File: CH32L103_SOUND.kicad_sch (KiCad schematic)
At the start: 44 parts, among them J1 USB_C_Receptacle_PowerOnly_6P, J2 Conn_01x04, J3 Conn_01x05, J4 Conn_01x02, Q1 AO3400A, U1 USBLC6-2SC6, U2 TP4057, U3 HT7533-1, U4 CS588, U5 CH32L103F8U6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

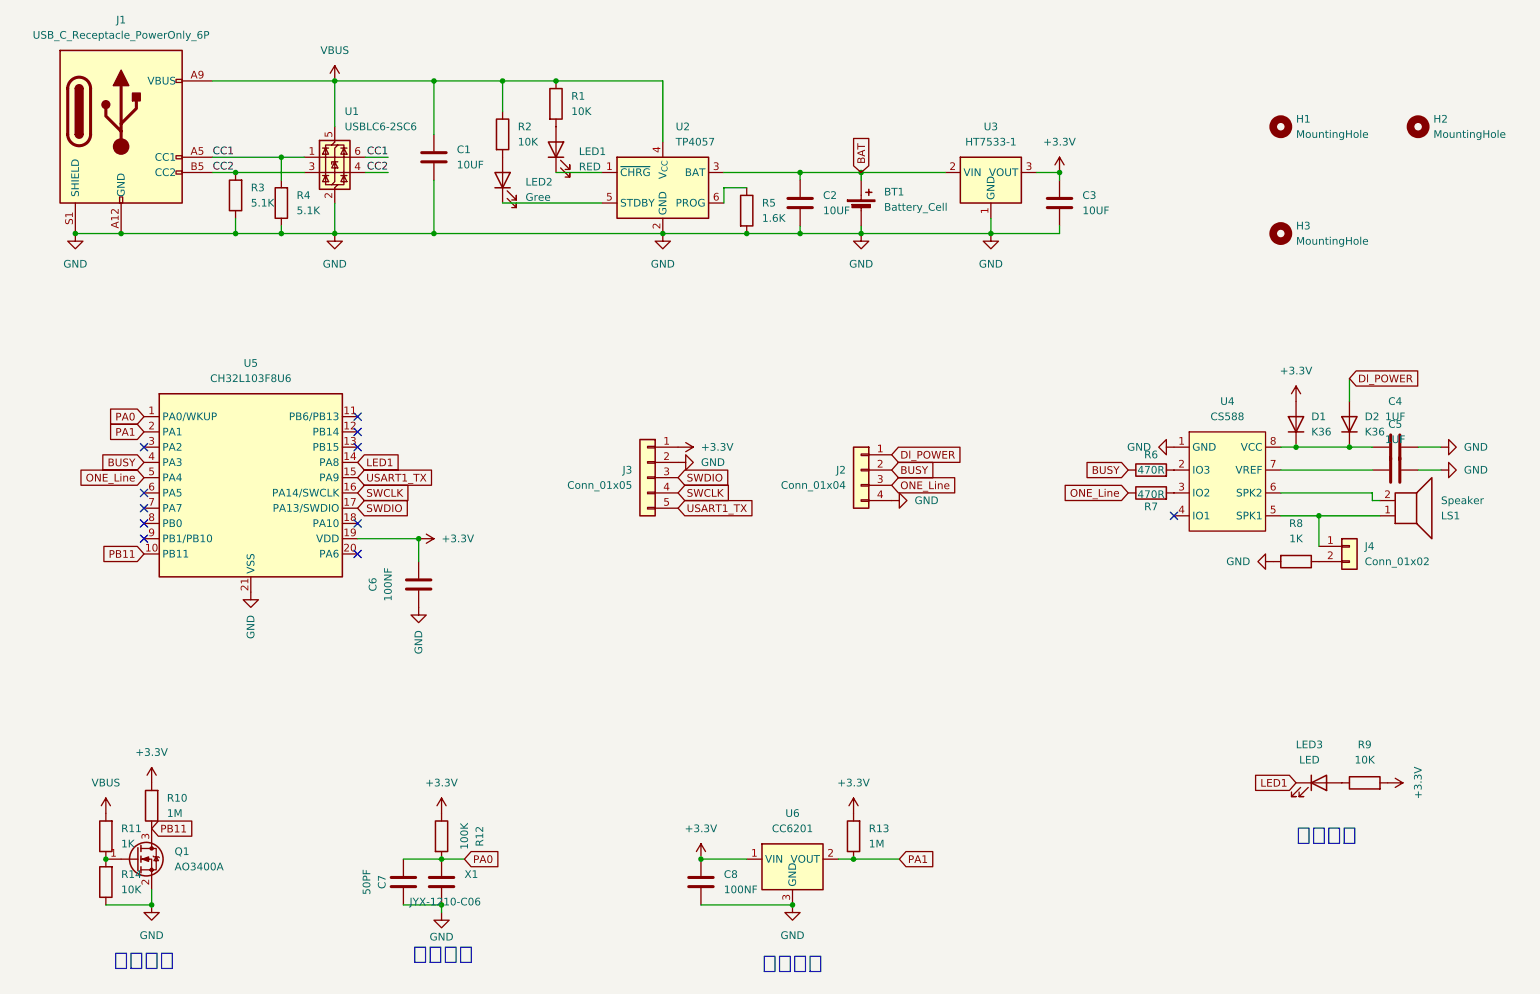
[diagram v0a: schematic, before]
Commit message: 修改引脚布局
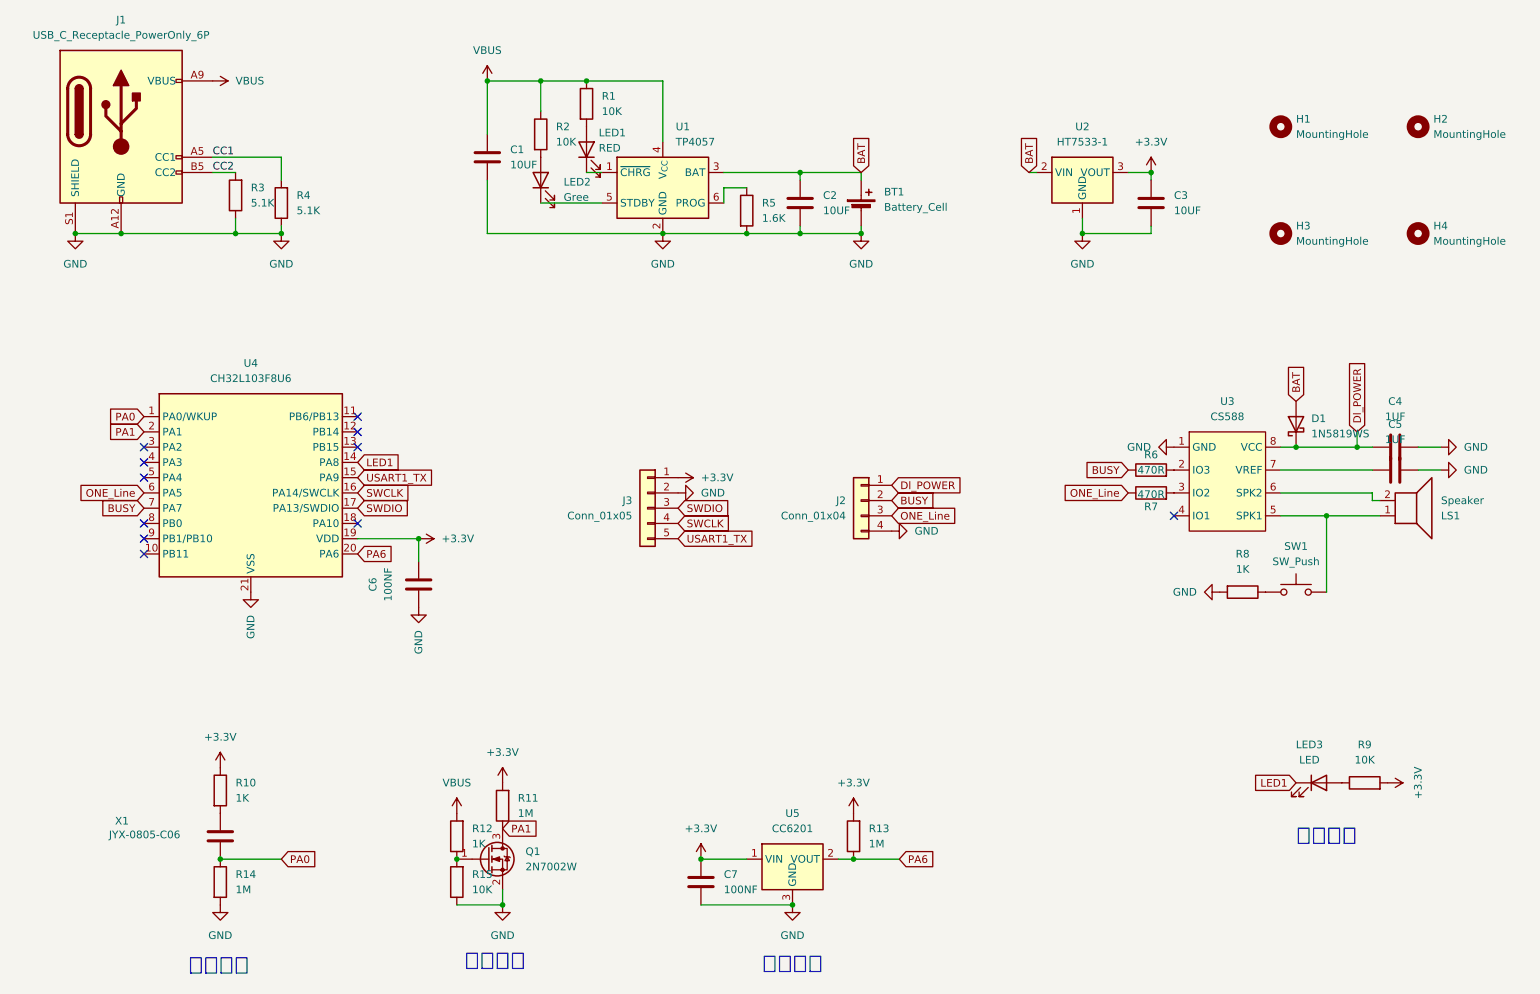
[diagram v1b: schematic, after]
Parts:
- removed C7: 50PF, Capacitor_SMD:C_0603_1608Metric, symbol Device:C
- removed D1, D2: K36, Diode_SMD:D_SOD-123F, symbol Device:D
- removed J4: Conn_01x02, Connector_PinHeader_2.54mm:PinHeader_1x02_P2.54mm_Vertical, symbol Connector_Generic:Conn_01x02
- removed Q1: AO3400A, Package_TO_SOT_SMD:SOT-23, symbol Transistor_FET:AO3400A
- removed R12: 100K, Resistor_SMD:R_0603_1608Metric, symbol Device:R
- removed U1: USBLC6-2SC6, Package_TO_SOT_SMD:SOT-23-6, symbol Power_Protection:USBLC6-2SC6
- added D1: 1N5819WS, Diode_SMD:D_SOD-323, symbol Diode:1N5819WS
- added H4: MountingHole, MountingHole:MountingHole_2.2mm_M2_ISO14580, symbol Mechanical:MountingHole
- added Q1: 2N7002W, Package_TO_SOT_SMD:SOT-323_SC-70, symbol Transistor_FET:2N7002
- added R10: 1K, Resistor_SMD:R_0402_1005Metric, symbol Device:R
- added R14: 1M, Resistor_SMD:R_0402_1005Metric, symbol Device:R
- added SW1: SW_Push, Maiooo_Library:Button_2P, symbol Switch:SW_Push
- C1, C2, C3: footprint Capacitor_SMD:C_0805_2012Metric -> Capacitor_SMD:C_0402_1005Metric
- C4, C5, C6: footprint Capacitor_SMD:C_0603_1608Metric -> Capacitor_SMD:C_0402_1005Metric
- C7: renamed from C8; footprint Capacitor_SMD:C_0603_1608Metric -> Capacitor_SMD:C_0402_1005Metric
- LED1, LED2, LED3: footprint LED_SMD:LED_0603_1608Metric -> LED_SMD:LED_0402_1005Metric
- R1, R13, R2, R3, R4, R5, R6, R7, R8, R9: footprint Resistor_SMD:R_0603_1608Metric -> Resistor_SMD:R_0402_1005Metric
- R11: renamed from R10; footprint Resistor_SMD:R_0603_1608Metric -> Resistor_SMD:R_0402_1005Metric
- R12: renamed from R11; footprint Resistor_SMD:R_0603_1608Metric -> Resistor_SMD:R_0402_1005Metric
- R15: renamed from R14; footprint Resistor_SMD:R_0603_1608Metric -> Resistor_SMD:R_0402_1005Metric
- U2: renamed from U3; footprint Package_TO_SOT_SMD:SOT-89-3 -> Maiooo_Library:HT7533s
- X1: value JYX-1210-C06 -> JYX-0805-C06; footprint Capacitor_SMD:C_1210_3225Metric -> Capacitor_SMD:C_0805_2012Metric
- renumbered U2 to U1, U4 to U3, U5 to U4, U6 to U5
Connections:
- net +3.3V: now also R10.1
- net BAT: now also D1.2 (A)
- net BUSY: now also U4.7 (PA7); no longer U4.4 (PA3)
- net Dl_POWER: now also C4.1, U3.8 (VCC), D1.1 (K)
- net GND: now also Q1.2 (S), R14.2; no longer X1.2
- net ONE_Line: now also U4.6 (PA5); no longer U4.5 (PA4)
- net PA0: now also X1.2, R14.1; no longer X1.1
- net PA1: now also R11.1, Q1.3 (D); no longer R13.1, U5.2 (VOUT)
- net at R12.1, R15.2: now also Q1.1 (G)
- net at LS1.1, U3.5 (SPK1): now also SW1.2
- net at R8.1: now also SW1.1
- net PA6: now reaches U4.20 (PA6)
- net PA6: now also R13.1, U5.2 (VOUT)
- net PB11: no longer names the net of U4.10 (PB11)
- net PB11: no longer R11.1
- new net: R10.2, X1.1
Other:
- moved on the sheet: C1, C3, J2, J3, LED1, LED2, R1, R11, R12, R15, R2, R8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

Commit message: 修改错误丝印
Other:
- note added: "LED指示灯"
- title: 震动语音公仔 -> (none)
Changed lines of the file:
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@@
 	(paper "A4")
 	(title_block
-		(title "震动语音公仔")
-		(date "2025-04-21")
-		(rev "1.1.0")
+		(date "2025-05-04")
+		(rev "1.2.0")
 		(company "Maiooo")
 	)
@@
 		)
 	)
-	(text "霍尔开关"
+	(text "LED指示灯"
 		(exclude_from_sim no)
 		(at 237.49 155.194 0)

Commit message: 新增注释
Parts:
- U3: value CS588 -> CX588
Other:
- note added: "CH32L03主控"
- note added: "CH32调试接口"
- note added: "CX588语音芯片"
- note added: "CX588调试接口"
- note added: "M2螺丝孔"
- note added: "USB-C 6Pin 充电接口"
- note added: "电池充电管理"
- note added: "线性稳压器"
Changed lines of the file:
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@@
 	(paper "A4")
 	(title_block
-		(date "2025-05-04")
+		(date "2025-05-12")
 		(rev "1.2.0")
 		(company "Maiooo")
@@
 		)
 	)
+	(text "M2螺丝孔"
+		(exclude_from_sim no)
+		(at 246.888 63.246 0)
+		(effects
+			(font
+				(size 2.54 2.54)
+			)
+		)
+	)
+	(text "电池充电管理"
+		(exclude_from_sim no)
+		(at 131.064 65.532 0)
+		(effects
+			(font
+				(size 2.54 2.54)
+			)
+		)
+	)
 	(text "LED指示灯"
 		(exclude_from_sim no)
@@
 		)
 	)
+	(text "线性稳压器"
+		(exclude_from_sim no)
+		(at 197.612 66.802 0)
+		(effects
+			(font
+				(size 2.54 2.54)
+			)
+		)
+	)
+	(text "CX588语音芯片"
+		(exclude_from_sim no)
+		(at 228.092 122.174 0)
+		(effects
+			(font
+				(size 2.54 2.54)
+			)
+		)
+	)
+	(text "CH32L03主控"
+		(exclude_from_sim no)
+		(at 58.42 126.746 0)
+		(effects
+			(font
+				(size 2.54 2.54)
+			)
+		)
+	)
+	(text "CH32调试接口"
+		(exclude_from_sim no)
+		(at 127 116.586 0)
+		(effects
+			(font
+				(size 2.54 2.54)
+			)
+		)
+	)
+	(text "USB-C 6Pin 充电接口"
+		(exclude_from_sim no)
+		(at 47.752 65.532 0)
+		(effects
+			(font
+				(size 2.54 2.54)
+			)
+		)
+	)
+	(text "CX588调试接口"
+		(exclude_from_sim no)
+		(at 165.354 115.57 0)
+		(effects
+			(font
+				(size 2.54 2.54)
+			)
+		)
+	)
 	(text "充电检测"
 		(exclude_from_sim no)
@@
 			)
 		)
-		(property "Value" "CS588"
+		(property "Value" "CX588"
 			(at 220.98 85.09 0)
 			(effects
